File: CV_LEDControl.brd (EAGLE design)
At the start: 48.2 x 28.3 mm, 7 parts, among them T1 2N2102

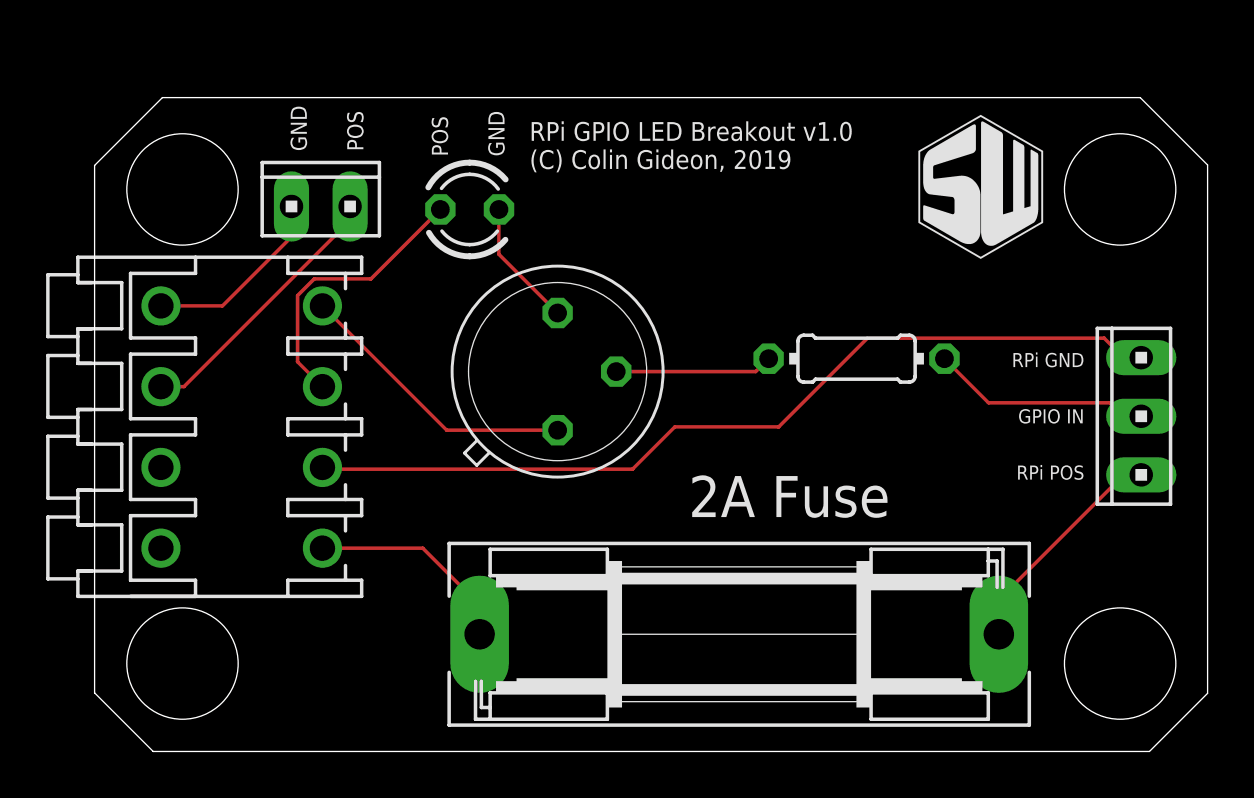
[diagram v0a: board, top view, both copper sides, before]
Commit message: Updated files to fix hole spacing and RPi output layout
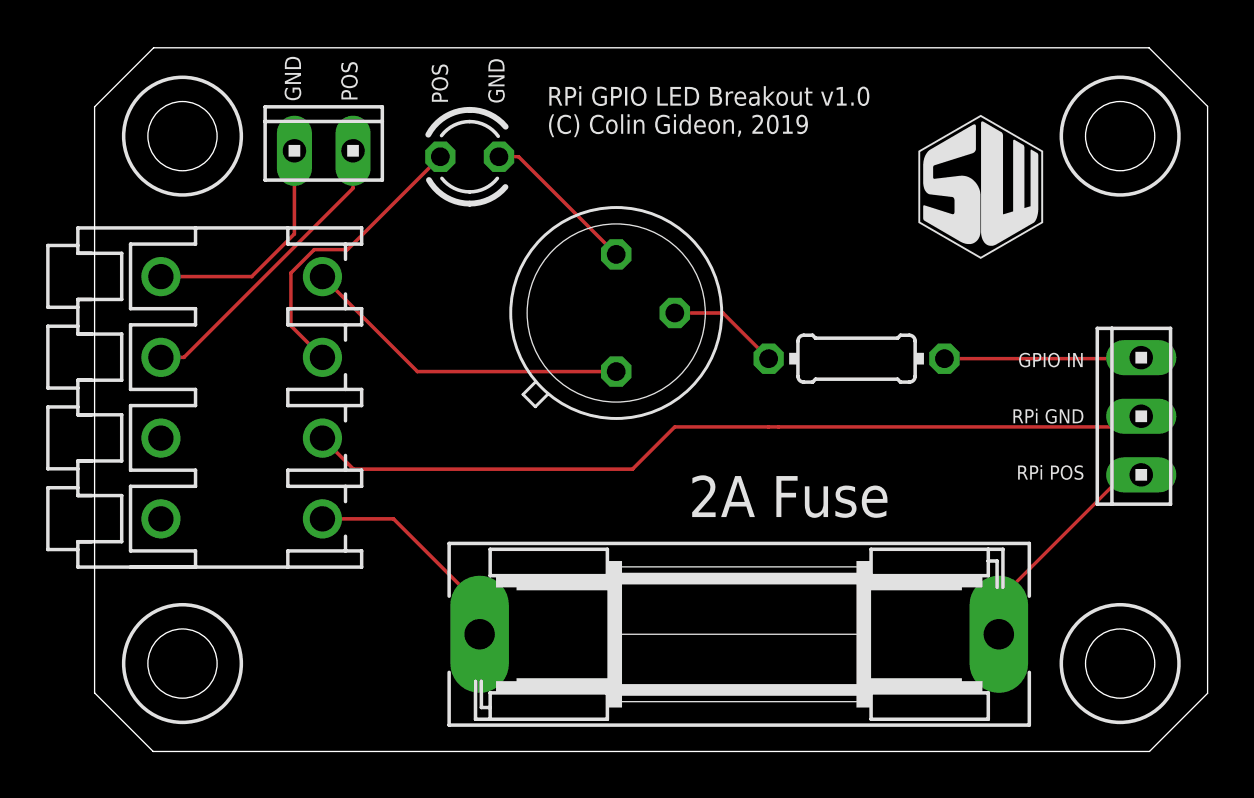
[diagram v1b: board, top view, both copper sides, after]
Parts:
- moved T1 3.59 mm to (22.6, 19.0)
- moved J2 2.42 mm to (9.93, 26.0)
- moved LED1 2.29 mm to (16.3, 25.8)
- moved E1 1.27 mm to (4.78, 15.3)
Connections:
- net N$2: now also J1.1; no longer J1.2
- net N$7: now also J1.2; no longer J1.1
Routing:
- net N$10: track 12.4 -> 14.4 mm
- net N$1: track 6.84 -> 4.89 mm
- net N$9: track 8.22 -> 10.2 mm
- net N$4: track 5.54 -> 6.84 mm
- net N$7: track 38.2 -> 37.0 mm
- net N$8: track 11.8 -> 13.0 mm
- net N$2: track 9.56 -> 8.55 mm
- net N$5: track 12.1 -> 12.8 mm
- net N$3: track 9.10 -> 9.63 mm
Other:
- board size 48.2 x 28.3 mm -> 48.2 x 30.5 mm
- board text added: "GPIO IN RPi GND RPi POS"
- board text removed: "RPi GND GPIO IN RPi POS"
